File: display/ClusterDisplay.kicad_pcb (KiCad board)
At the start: 4 copper layers, 229.5 x 114 mm, 76 parts, among them J1 Verdin iMX95, J10 RTC coin cell, J2 Power in, J3 CAN to ECU, J4 DM-TFTR50-413 panel, J8 JTAG debug, J9 Buttons, Q1 NFET diode, Q2 NFET pass, Q3 MFT6N2A5S23A (AEC-Q101, 60V/2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, U1 LM74930-Q1, U2 LM61460-Q1, U3 TLV767-Q1, U4 TCAN1044V-Q1, U6 TPS60403-Q1, U7 AL8853AQ

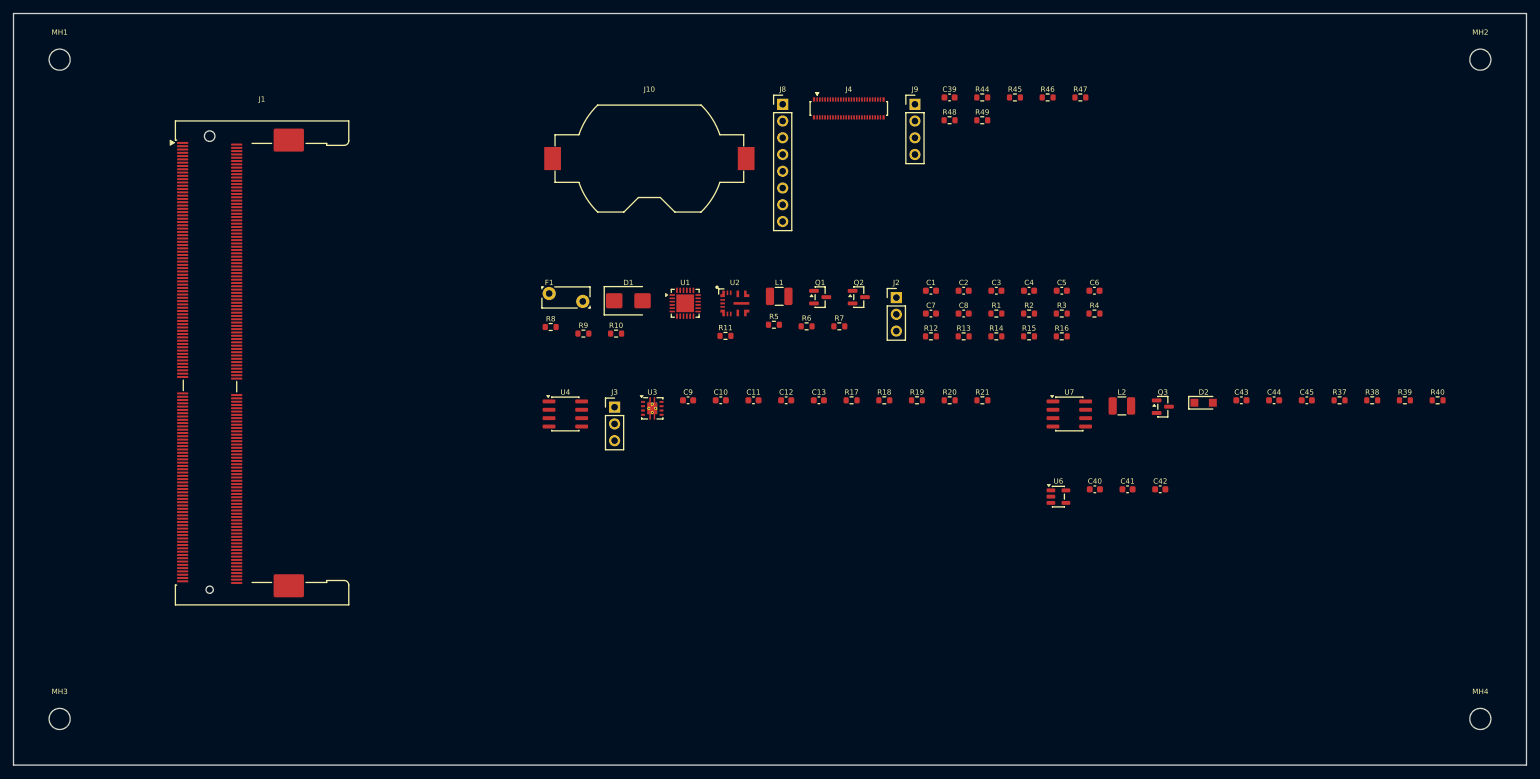
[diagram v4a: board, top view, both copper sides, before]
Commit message: display: real Toradex module keepout numbers, pack for min width not height
Pulled Toradex's own Verdin Carrier Board Design Guide (docs.toradex.com/
108140-verdin-carrier-board-design-guide.pdf) directly and read Figure
110 (module outline) and Figure 114 (carrier board land pattern) rather
than continuing to guess. Two real corrections:

1. The module is 69.60 x 35.00mm, not 69.6 x 47mm - the 47mm figure
   came from an earlier, less authoritative web source. The module
   overhangs the connector's own real 27.1mm body by ~4mm/side on the
   width axis (confirmed centered, not assumed) and does NOT overhang
   it lengthwise (the connector's own 79mm housing is longer than the
   69.6mm module). MODULE_KEEPOUT_W drops from 60mm to a real 38mm;
   MODULE_KEEPOUT_H stays ~82mm (already correctly sized off the
   connector's real housing length).

2. pack_sized_blocks() was bounding WIDTH and growing height freely,
   then a later step stretched that height back out to fill the
   module's real height anyway - meaning the packer was minimizing a
   dimension that gets thrown away, while the dimension that actually
   sets board size (width) fell out however the internal ordering
   happened to land. Transposed the call instead: bound at the real
   module height, let width grow only as needed, swap the result back.

Board: 231.9x114.0mm -> 158.0x106.0mm, DRC-clean. Real, cited numbers
throughout - see the file's own updated header and MODULE_KEEPOUT
comments for the derivation.

Co-Authored-By: Claude Sonnet 5 <noreply@anthropic.com>
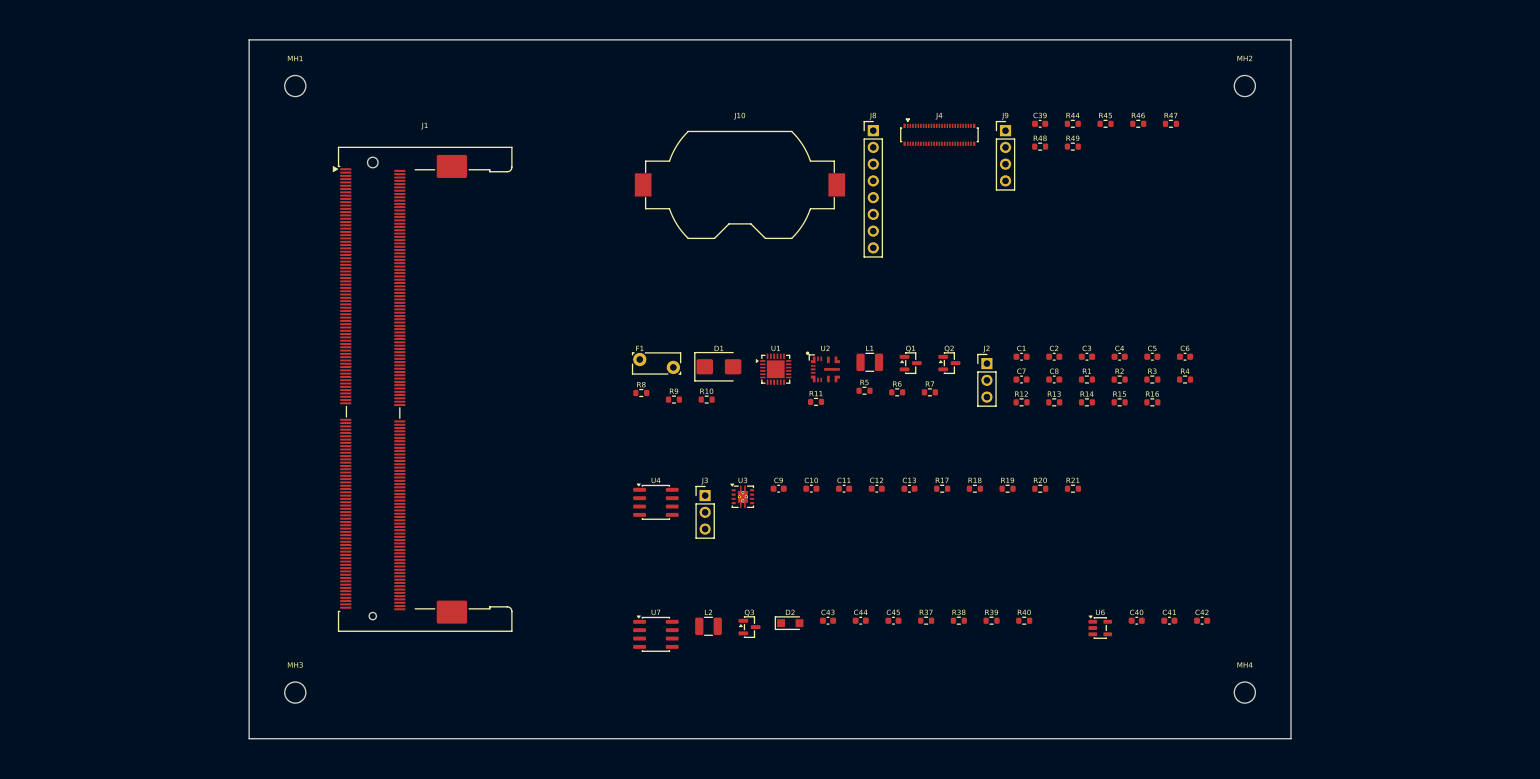
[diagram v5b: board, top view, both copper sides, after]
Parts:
- moved C45 71.1 mm to (228.7, 183.6)
- moved L2 71.1 mm to (200.7, 184.4)
- moved R39 71.1 mm to (243.6, 183.6)
- moved C43 71.1 mm to (218.8, 183.6)
- moved C44 71.1 mm to (223.8, 183.6)
- moved D2 71.1 mm to (213.1, 184.0)
- moved Q3 71.1 mm to (206.9, 184.6)
- moved R37 71.1 mm to (233.7, 183.6)
- moved R38 71.1 mm to (238.6, 183.6)
- moved R40 71.1 mm to (248.6, 183.6)
- moved U7 71.1 mm to (192.7, 185.7)
- moved MH1 36.0 mm to (138.0, 102.5)
- moved MH3 36.0 mm to (138.0, 194.5)
- moved MH2 35.9 mm to (282.0, 102.5)
- moved MH4 35.9 mm to (282.0, 194.5)
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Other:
- board size 229.5 x 114 mm -> 158 x 106 mm

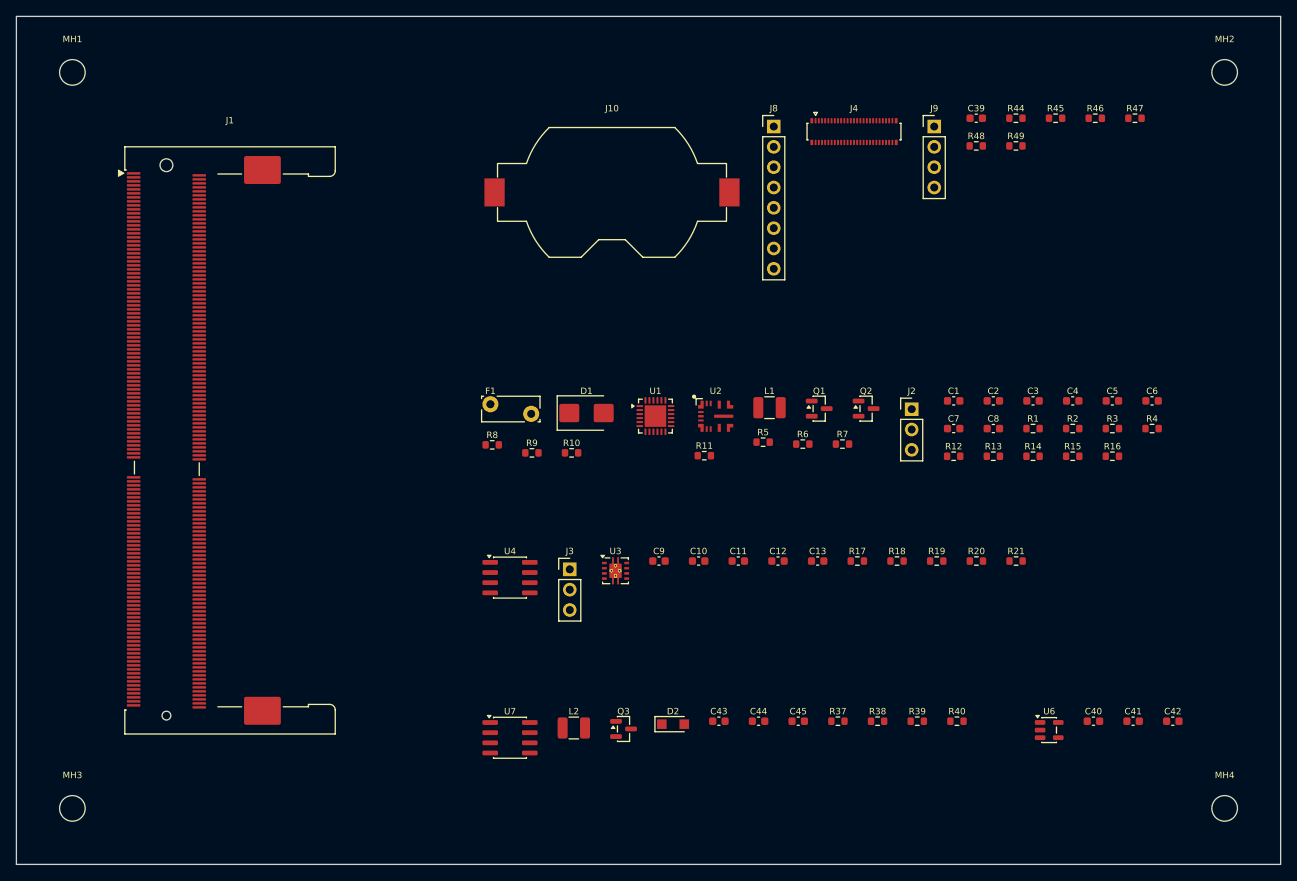
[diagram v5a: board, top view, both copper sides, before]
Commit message: display: flatten zone-block packing to individual-component packing
Direct user tradeoff: "break zone grouping for max density." The
previous zone-block approach (each of the 5 functional zones packed
internally, then the resulting rectangles packed around the module
keepout) hit a real floor - board width couldn't shrink below the
single widest zone's own packed width (POWER, 85.4mm) no matter how
the zones were arranged relative to each other, since each was shaped
into one rigid block before ever being placed.

Replaced zone-block packing with a flat pack of all 72 individual real
components directly, using the same transposed skyline technique
(bound at the module's real 82mm height, minimize width) via a
generalized pack_sized_blocks(). CORE_ZONES is kept for documentation
and the "every part is accounted for" check, but no longer drives
placement - components from different zones now interleave on the
board. skyline_pack()/best_skyline_pack() are now dead code (nothing
loads per-zone footprints anymore) - removed.

Board: 158.0x106.0mm -> 105.0x106.0mm, DRC-clean. Real, accepted
tradeoff: a part may now sit farther from the rest of its own circuit
than before, since density was explicitly prioritized over that
locality.

Co-Authored-By: Claude Sonnet 5 <noreply@anthropic.com>
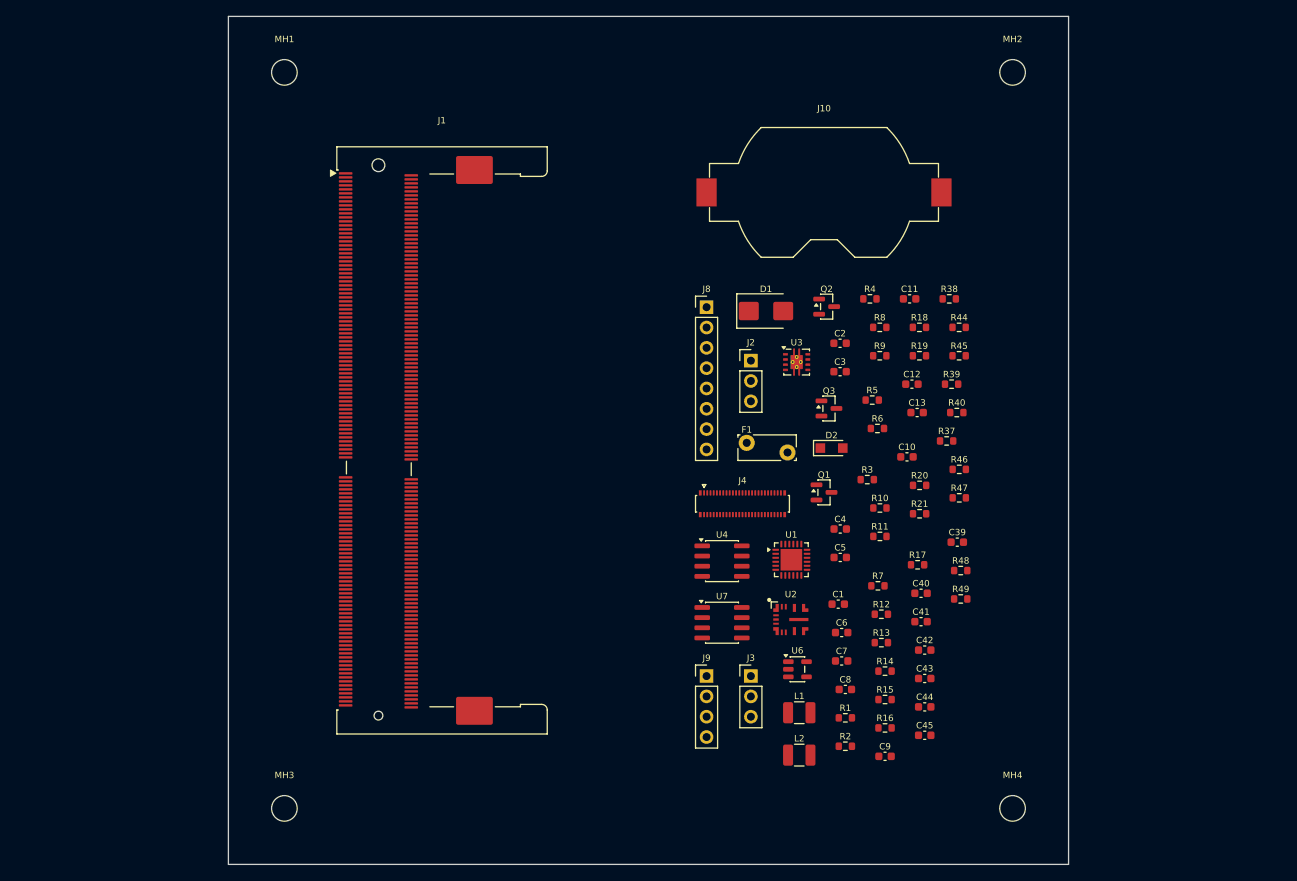
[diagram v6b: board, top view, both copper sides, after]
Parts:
- moved J9 74.4 mm to (217.3, 178.0)
- moved R49 57.0 mm to (249.0, 168.3)
- moved R38 53.5 mm to (247.6, 130.8)
- moved R48 53.1 mm to (249.0, 164.8)
- moved C39 53.0 mm to (248.6, 161.2)
- moved R47 52.3 mm to (248.8, 155.7)
- moved R8 50.6 mm to (238.9, 134.4)
- moved R2 48.8 mm to (234.6, 186.7)
- moved J4 48.6 mm to (221.8, 156.4)
- moved C6 48.4 mm to (234.2, 172.5)
- moved Q3 47.6 mm to (232.6, 144.5)
- moved R46 47.1 mm to (248.8, 152.1)
- moved R9 45.1 mm to (238.9, 137.9)
- moved R16 44.3 mm to (239.6, 184.4)
- moved R1 43.1 mm to (234.6, 183.2)
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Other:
- board size 158 x 106 mm -> 105 x 106 mm

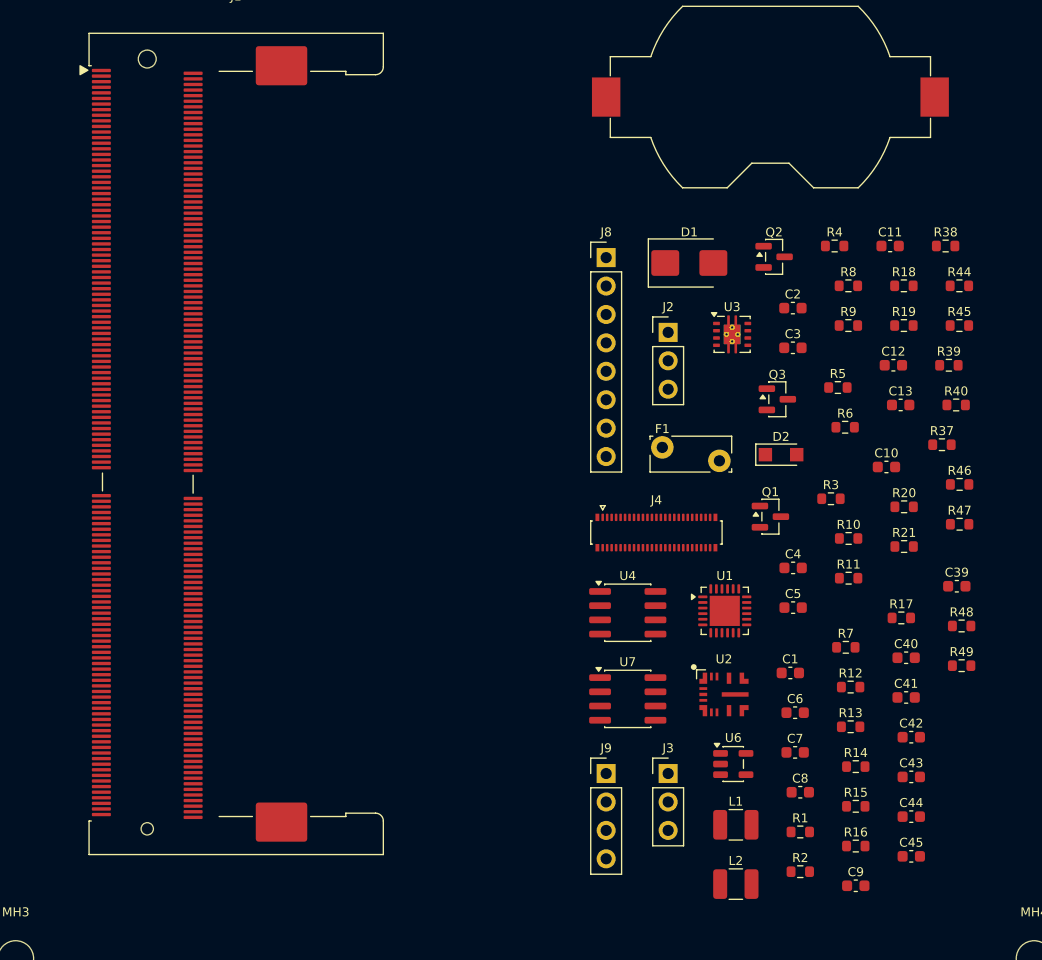
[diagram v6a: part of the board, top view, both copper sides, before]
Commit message: display: route board and generate real BOM
Added +12V_PROT trunk-widening constants (TRUNK_WIDTH_LADDER/
TRUNK_NETS) to build_pcb.py - this board's own real fused/protected
rail, feeding both the main +5V buck and the backlight boost converter,
so it's sized toward F1's real 5A rating rather than reusing gauges/'s
smaller 2A-fuse ladder.

Routed ClusterDisplay.kicad_pcb with FreeRouting (0 unrouted on the
first attempt) plus post-route GND/+5V zone pours (this board has no
+3V3 net - +5V is the real widely-distributed second rail here) and
+12V_PROT trunk widening, adapted from gauges/route_board.py. Same real
TRACK_CLEARANCE fix applied (0.15 -> 0.2, see gauges/route_board.py's
own comment for the full real DRC evidence).

Fixed a real value-spelling bug caught by build_bom.py's own check:
R39 was written as "10.0k" while the identical 10k pullups (R21, R44-
R48) were written "10k" - same real part, split into two BOM lines by
spelling alone. Normalized to "10k" (the OVP divider's ~25% real
margin doesn't call for a tighter tolerance than the default), then
regenerated schematic -> PCB -> re-routed (footprint/net-only pipeline,
reproduced the identical 105.0x106.0mm layout as expected).

Added build_bom.py, same real generated-BOM discipline as gauges/'s
own - this board has more genuine "needs real part selection" lines
(Q1/Q2 front-end FETs, D1 TVS, F1's exact fuse suffix, J1's exact
Verdin SKU, J2/J3/J8/J9's provisional headers) since the AAOS pivot
that created it only landed 2 days ago; each is flagged honestly
rather than given a fabricated-precise part number. 72/72 real parts
covered (after fixing a real multi-unit-symbol double-count in
load_parts() - J1's Verdin X1 connector is split into 7 real schematic
units sharing one Reference, which a naive one-entry-per-symbol-
instance count would silently double-count 7x).

Co-Authored-By: Claude Sonnet 5 <noreply@anthropic.com>
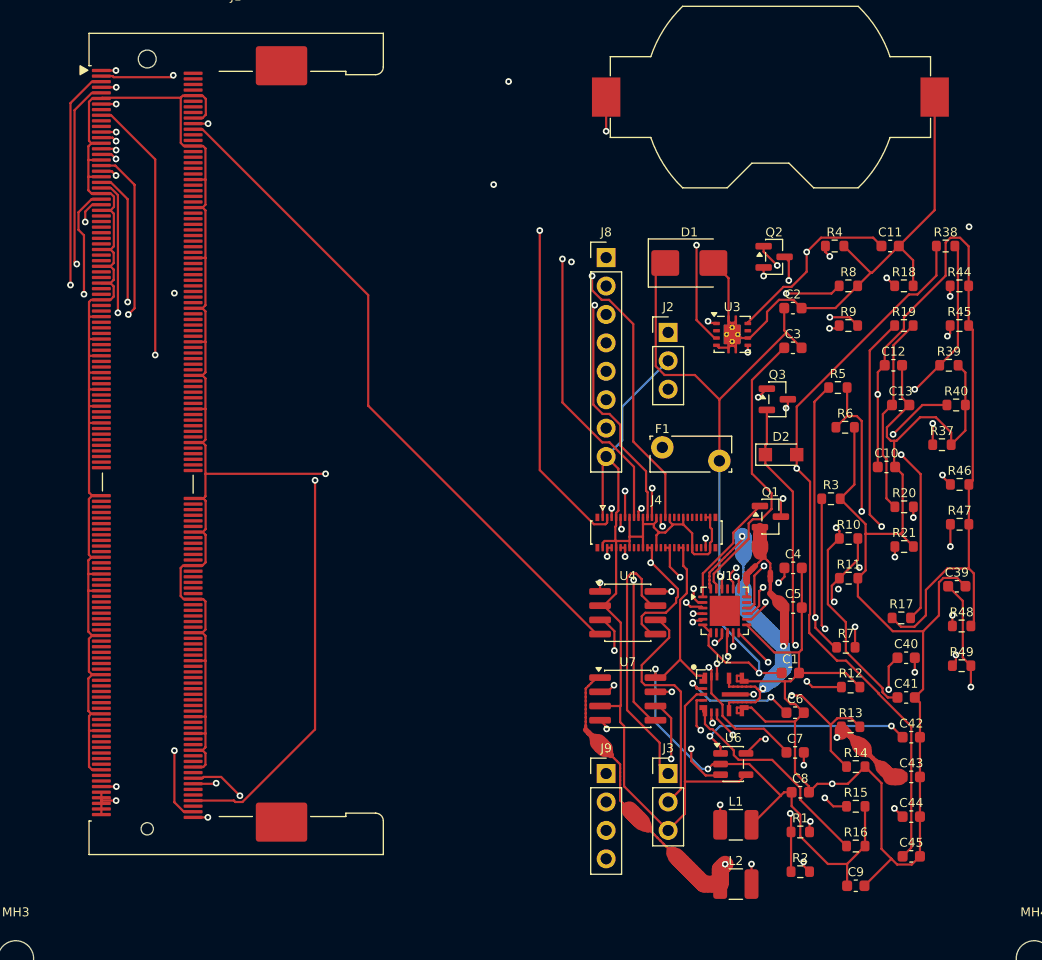
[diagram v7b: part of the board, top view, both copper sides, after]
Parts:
- R39: value 10.0k OVP bottom (real, see docstring math) -> 10k OVP bottom (real, see docstring math)
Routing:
- net GND: track 0.00 -> 565.0 mm, vias 0 -> 2
- net +5V: track 0.00 -> 209.5 mm, vias 0 -> 6
- net +1V8: track 0.00 -> 125.1 mm, vias 0 -> 3
- net +12V_PROT: track 0.00 -> 111.1 mm, vias 0 -> 5
- net RESET_MICO: track 0.00 -> 108.2 mm, vias 0 -> 2
- net JTAG_VREF: track 0.00 -> 107.2 mm, vias 0 -> 2
- net PWR_BTN: track 0.00 -> 95.4 mm, vias 0 -> 2
- net VBAT_F: track 0.00 -> 95.3 mm, vias 0 -> 3
- net RECOVERY: track 0.00 -> 93.3 mm, vias 0 -> 2
- net VBACKUP: track 0.00 -> 91.4 mm, vias 0 -> 2
- net RESET_MOCI: track 0.00 -> 85.5 mm, vias 0 -> 2
- net PANEL_BL_LEDA_38V: track 0.00 -> 85.1 mm, vias 0 -> 2
- net DSI_PANEL_EN: track 0.00 -> 80.7 mm, vias 0 -> 2
- net PWR_EN_MOCI: track 0.00 -> 80.2 mm, vias 0 -> 2
- net VBACKUP_CELL: track 0.00 -> 78.9 mm, vias 0 -> 3
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- added copper zone on In2.Cu, net +5V
- added copper zone on In1.Cu, net GND
